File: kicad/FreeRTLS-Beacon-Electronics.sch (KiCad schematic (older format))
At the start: 28 parts, among them J1 USB_B_Micro, J2 TC2030, U1 STM32F072CBTx, U2 AZ1117IH-3.3TRG1, U3 DWM1001

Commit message: Add license info in page settings
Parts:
- D3, D5: Manufacturer Wurth Elektronik -> Würth Elektronik
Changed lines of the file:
@@
 Rev "WIP!"
 Comp "FreeRTLS"
-Comment1 "Revisor: Luciano Vittori"
-Comment2 "Author: David Broin"
-Comment3 ""
-Comment4 ""
+Comment1 ""
+Comment2 "CERN Open Hardware Licence Version 2 - Permissive"
+Comment3 "Revisor: Luciano Vittori"
+Comment4 "Author: David Broin"
 $EndDescr
 $Comp
@@
 F 5 "732-4978-1-ND" H 3900 1600 50  0001 C CNN "Digi-Key_PN"
 F 6 "150060RS75000" H 3900 1600 50  0001 C CNN "MPN"
-F 7 "Wurth Elektronik" H 3900 1600 50  0001 C CNN "Manufacturer"
+F 7 "Würth Elektronik" H 3900 1600 50  0001 C CNN "Manufacturer"
 	1    3900 1600
 	0    -1   -1   0
@@
 F 5 "732-4971-1-ND" H 2150 4850 50  0001 C CNN "Digi-Key_PN"
 F 6 "150060GS75000" H 2150 4850 50  0001 C CNN "MPN"
-F 7 "Wurth Elektronik" H 2150 4850 50  0001 C CNN "Manufacturer"
+F 7 "Würth Elektronik" H 2150 4850 50  0001 C CNN "Manufacturer"
 	1    2150 4850
 	0    -1   -1   0

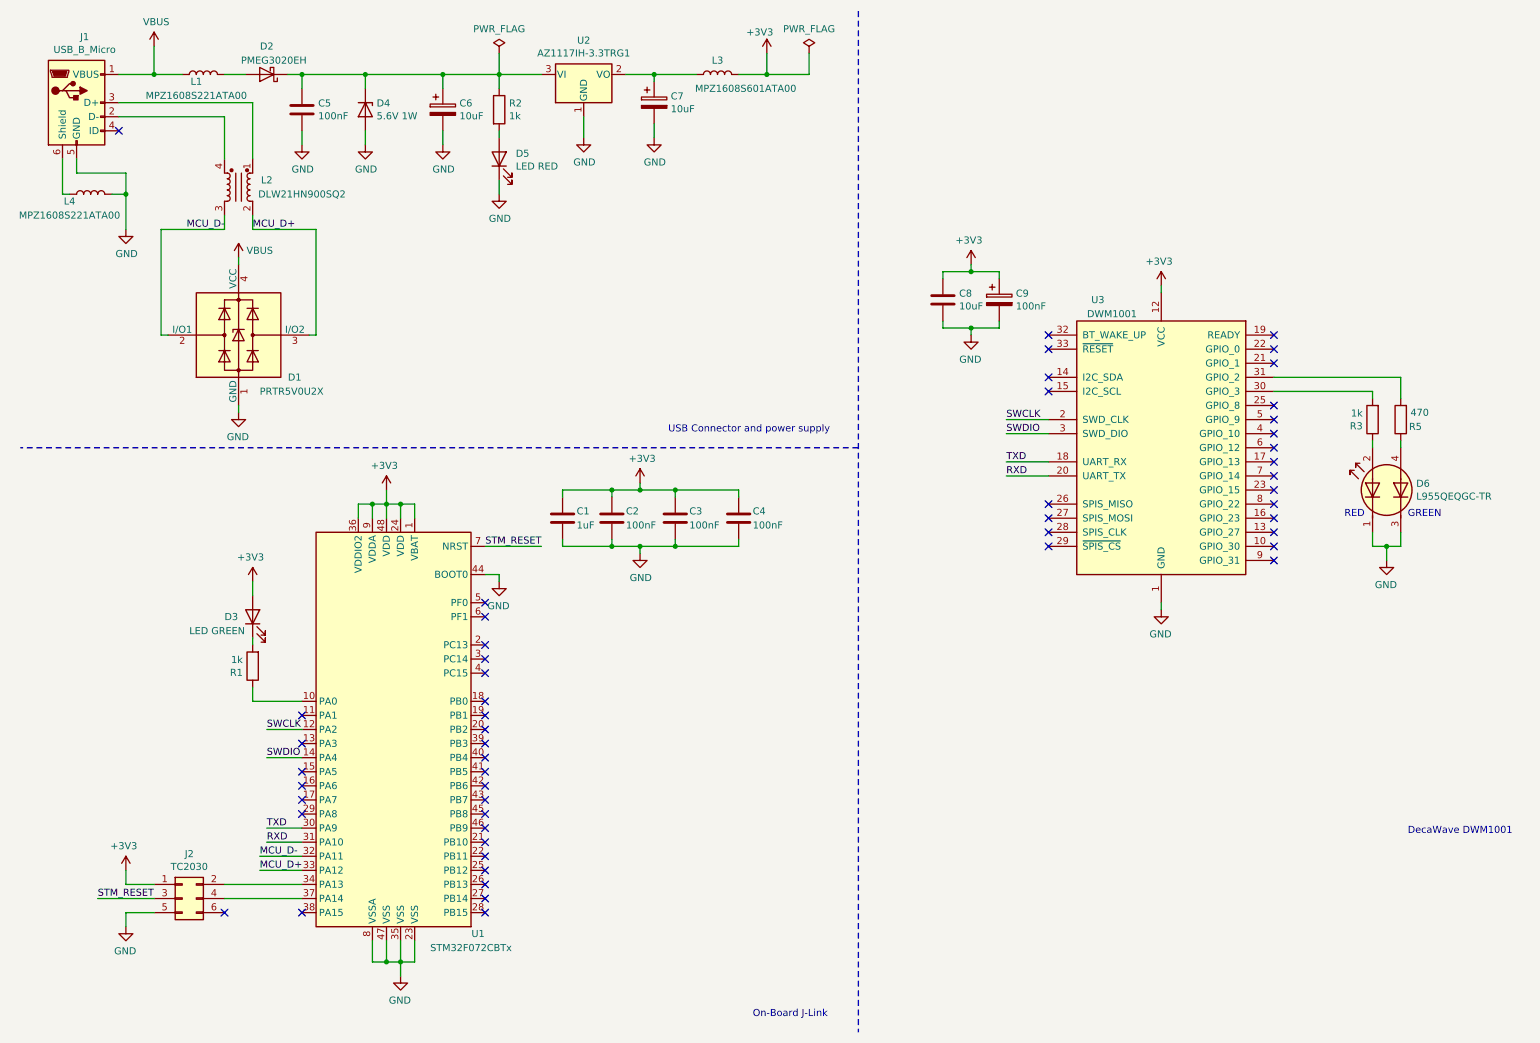
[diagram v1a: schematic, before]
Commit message: Add mounting holes and fiducials
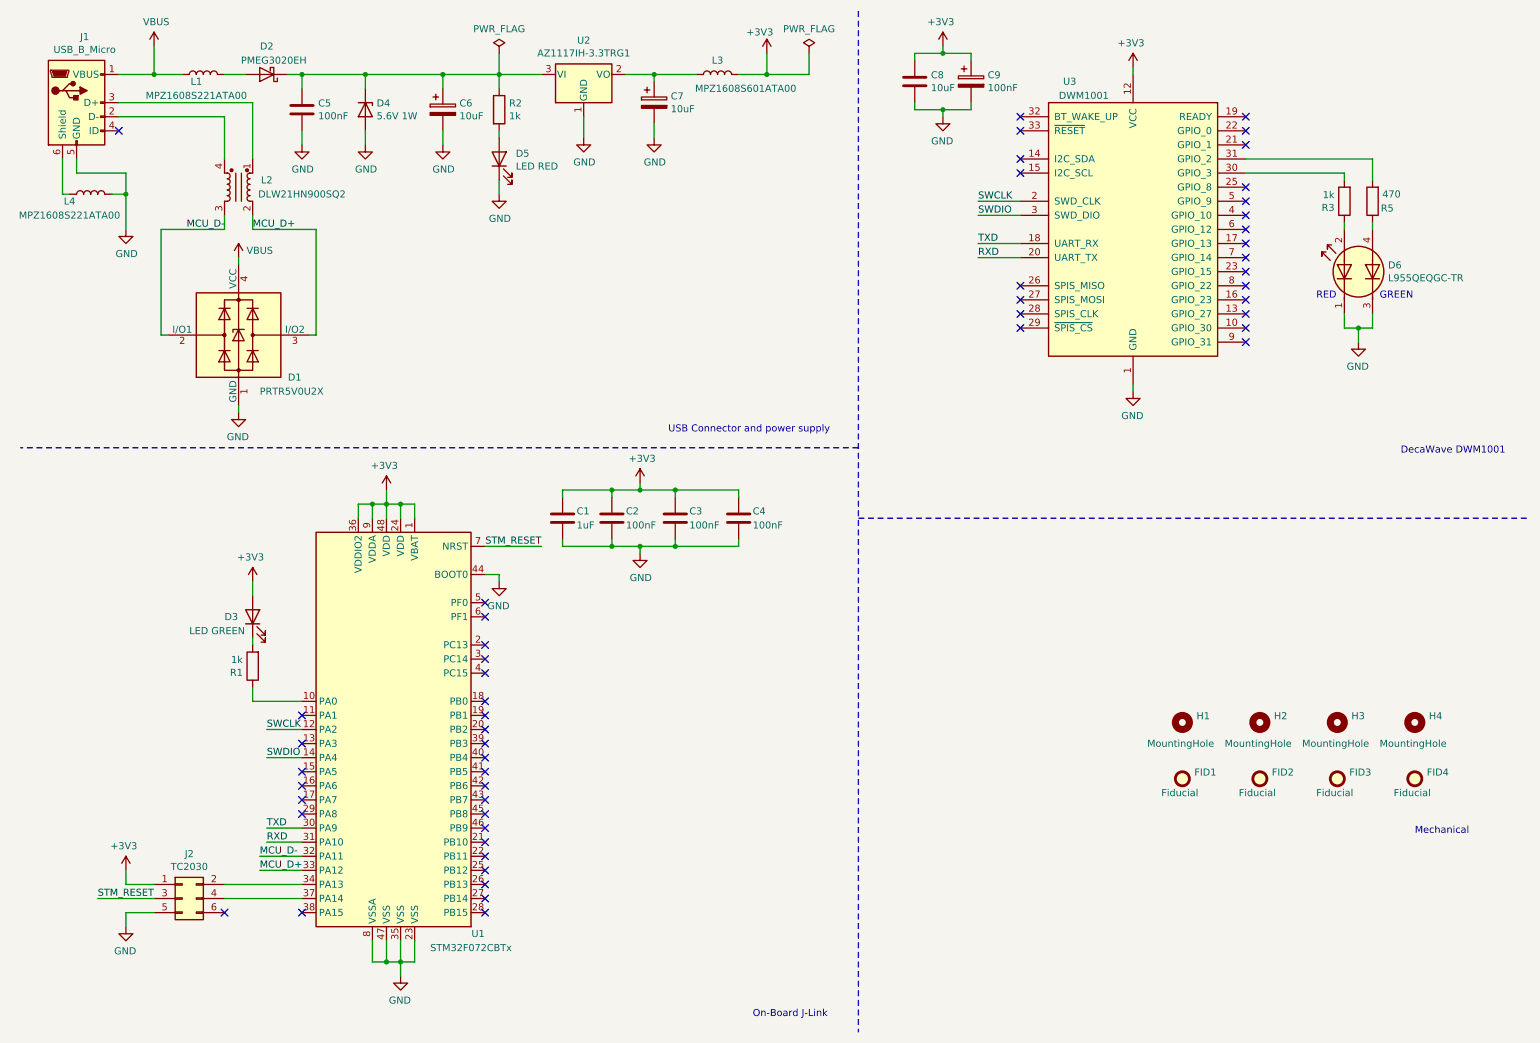
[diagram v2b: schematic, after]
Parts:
- added FID1, FID2, FID3: Fiducial, Fiducial:Fiducial_0.5mm_Mask1.5mm, symbol Mechanical:Fiducial
- added FID4: Fiducial, MountingHole:MountingHole_3.2mm_M3, symbol Mechanical:Fiducial
- added H1, H2, H3, H4: MountingHole, MountingHole:MountingHole_3.2mm_M3, symbol Mechanical:MountingHole
- D3, D5: Manufacturer Würth Elektronik -> Wurth Elektronik
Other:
- note added: "Mechanical"
- moved on the sheet: C8, C9, D6, R3, R5, U3

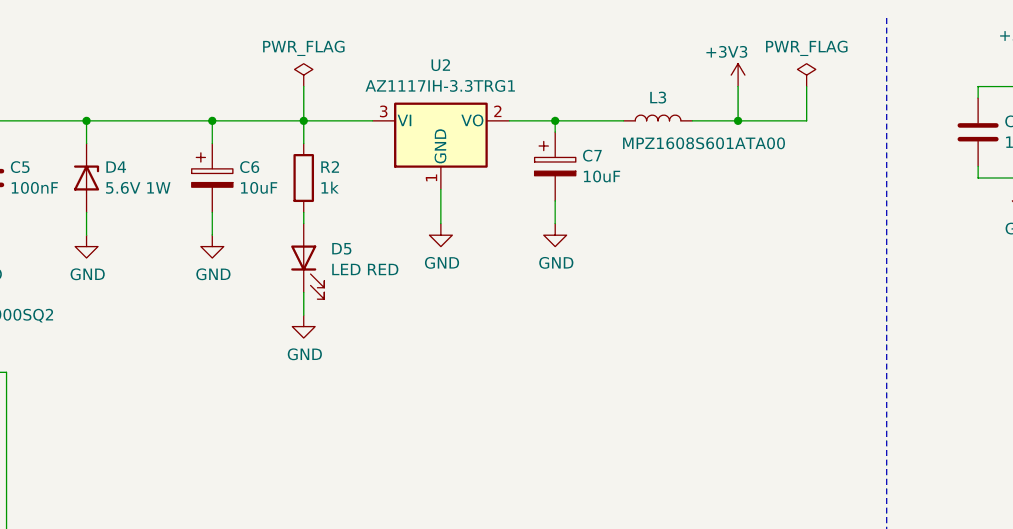
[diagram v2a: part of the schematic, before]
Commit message: Move LED to 3v3 to test whole power
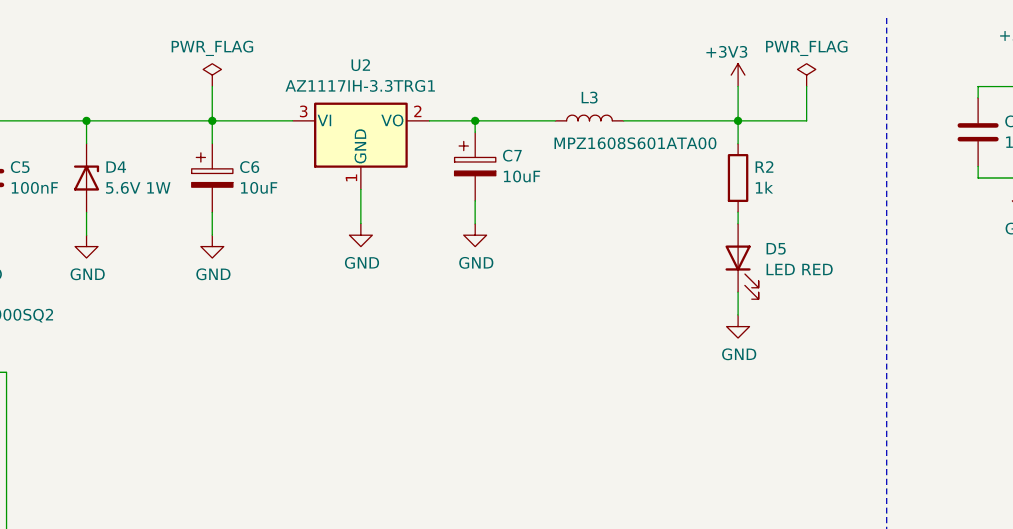
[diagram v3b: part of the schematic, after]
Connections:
- net +3V3: now also R2.1
- net at C5.1, C6.1, D2.1 (K)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: no longer R2.1
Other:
- moved on the sheet: C7, D5, L3, R2, U2
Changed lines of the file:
@@
 L Regulator_Linear:NCP1117-3.3_SOT223 U2
 U 1 1 5F4F1B06
-P 4500 1000
-F 0 "U2" H 4500 1242 50  0000 C CNN
-F 1 "AZ1117IH-3.3TRG1" H 4500 1151 50  0000 C CNN
-F 2 "Package_TO_SOT_SMD:SOT-223-3_TabPin2" H 4500 1200 50  0001 C CNN
-F 3 "https://www.diodes.com/assets/Datasheets/AZ1117I.pdf" H 4600 750 50  0001 C CNN
-F 4 "https://www.digikey.com/en/products/detail/diodes-incorporated/AZ1117IH-3-3TRG1/5699672" H 4500 1000 50  0001 C CNN "DK_Detail_Page"
-F 5 "AZ1117IH-3.3TRG1DICT-ND" H 4500 1000 50  0001 C CNN "Digi-Key_PN"
-F 6 "AZ1117IH-3.3TRG1" H 4500 1000 50  0001 C CNN "MPN"
-F 7 "Diodes Incorporated" H 4500 1000 50  0001 C CNN "Manufacturer"
-	1    4500 1000
+P 4150 1000
+F 0 "U2" H 4150 1242 50  0000 C CNN
+F 1 "AZ1117IH-3.3TRG1" H 4150 1151 50  0000 C CNN
+F 2 "Package_TO_SOT_SMD:SOT-223-3_TabPin2" H 4150 1200 50  0001 C CNN
+F 3 "https://www.diodes.com/assets/Datasheets/AZ1117I.pdf" H 4250 750 50  0001 C CNN
+F 4 "https://www.digikey.com/en/products/detail/diodes-incorporated/AZ1117IH-3-3TRG1/5699672" H 4150 1000 50  0001 C CNN "DK_Detail_Page"
+F 5 "AZ1117IH-3.3TRG1DICT-ND" H 4150 1000 50  0001 C CNN "Digi-Key_PN"
+F 6 "AZ1117IH-3.3TRG1" H 4150 1000 50  0001 C CNN "MPN"
+F 7 "Diodes Incorporated" H 4150 1000 50  0001 C CNN "Manufacturer"
+	1    4150 1000
 	1    0    0    -1
 $EndComp
@@
 	3500 1100 3500 1000
 Connection ~ 3500 1000
-Wire Wire Line
-	3500 1000 3900 1000
 $Comp
 L Device:R R2
 U 1 1 5F4F80D3
-P 3900 1250
-F 0 "R2" H 3970 1296 50  0000 L CNN
-F 1 "1k" H 3970 1205 50  0000 L CNN
-F 2 "Resistor_SMD:R_0603_1608Metric" V 3830 1250 50  0001 C CNN
-F 3 "~" H 3900 1250 50  0001 C CNN
-F 4 "https://www.digikey.com/en/products/detail/yageo/RC0603JR-071KL/726677" H 3900 1250 50  0001 C CNN "DK_Detail_Page"
-F 5 "311-1.0KGRCT-ND" H 3900 1250 50  0001 C CNN "Digi-Key_PN"
-F 6 "RC0603JR-071KL" H 3900 1250 50  0001 C CNN "MPN"
-F 7 "Yageo" H 3900 1250 50  0001 C CNN "Manufacturer"
-	1    3900 1250
+P 5800 1250
+F 0 "R2" H 5870 1296 50  0000 L CNN
+F 1 "1k" H 5870 1205 50  0000 L CNN
+F 2 "Resistor_SMD:R_0603_1608Metric" V 5730 1250 50  0001 C CNN
+F 3 "~" H 5800 1250 50  0001 C CNN
+F 4 "https://www.digikey.com/en/products/detail/yageo/RC0603JR-071KL/726677" H 5800 1250 50  0001 C CNN "DK_Detail_Page"
+F 5 "311-1.0KGRCT-ND" H 5800 1250 50  0001 C CNN "Digi-Key_PN"
+F 6 "RC0603JR-071KL" H 5800 1250 50  0001 C CNN "MPN"
+F 7 "Yageo" H 5800 1250 50  0001 C CNN "Manufacturer"
+	1    5800 1250
 	1    0    0    -1
 $EndComp
@@
 L Device:LED D5
 U 1 1 5F4F882D
-P 3900 1600
-F 0 "D5" V 3939 1482 50  0000 R CNN
-F 1 "LED RED" V 3848 1482 50  0000 R CNN
-F 2 "LED_SMD:LED_0603_1608Metric_Castellated" H 3900 1600 50  0001 C CNN
-F 3 "~" H 3900 1600 50  0001 C CNN
-F 4 "https://www.digikey.com/en/products/detail/w%C3%BCrth-elektronik/150060RS75000/4489901" H 3900 1600 50  0001 C CNN "DK_Detail_Page"
-F 5 "732-4978-1-ND" H 3900 1600 50  0001 C CNN "Digi-Key_PN"
-F 6 "150060RS75000" H 3900 1600 50  0001 C CNN "MPN"
-F 7 "Wurth Elektronik" H 3900 1600 50  0001 C CNN "Manufacturer"
-	1    3900 1600
+P 5800 1600
+F 0 "D5" V 5839 1482 50  0000 R CNN
+F 1 "LED RED" V 5748 1482 50  0000 R CNN
+F 2 "LED_SMD:LED_0603_1608Metric_Castellated" H 5800 1600 50  0001 C CNN
+F 3 "~" H 5800 1600 50  0001 C CNN
+F 4 "https://www.digikey.com/en/products/detail/w%C3%BCrth-elektronik/150060RS75000/4489901" H 5800 1600 50  0001 C CNN "DK_Detail_Page"
+F 5 "732-4978-1-ND" H 5800 1600 50  0001 C CNN "Digi-Key_PN"
+F 6 "150060RS75000" H 5800 1600 50  0001 C CNN "MPN"
+F 7 "Wurth Elektronik" H 5800 1600 50  0001 C CNN "Manufacturer"
+	1    5800 1600
 	0    -1   -1   0
 $EndComp
 Wire Wire Line
-	3900 1100 3900 1000
-Connection ~ 3900 1000
-Wire Wire Line
-	3900 1000 4200 1000
-Wire Wire Line
-	3900 1400 3900 1450
+	5800 1100 5800 1000
+Wire Wire Line
+	3500 1000 3850 1000
+Wire Wire Line
+	5800 1400 5800 1450
 $Comp
 L power:GND #PWR011
@@
 L power:GND #PWR015
 U 1 1 5F4FA5A8
-P 3900 1850
-F 0 "#PWR015" H 3900 1600 50  0001 C CNN
-F 1 "GND" H 3905 1677 50  0000 C CNN
-F 2 "" H 3900 1850 50  0001 C CNN
-F 3 "" H 3900 1850 50  0001 C CNN
-	1    3900 1850
+P 5800 1850
+F 0 "#PWR015" H 5800 1600 50  0001 C CNN
+F 1 "GND" H 5805 1677 50  0000 C CNN
+F 2 "" H 5800 1850 50  0001 C CNN
+F 3 "" H 5800 1850 50  0001 C CNN
+	1    5800 1850
 	1    0    0    -1
 $EndComp
@@
 L power:GND #PWR016
 U 1 1 5F4FAA35
-P 4500 1450
-F 0 "#PWR016" H 4500 1200 50  0001 C CNN
-F 1 "GND" H 4505 1277 50  0000 C CNN
-F 2 "" H 4500 1450 50  0001 C CNN
-F 3 "" H 4500 1450 50  0001 C CNN
-	1    4500 1450
+P 4150 1450
+F 0 "#PWR016" H 4150 1200 50  0001 C CNN
+F 1 "GND" H 4155 1277 50  0000 C CNN
+F 2 "" H 4150 1450 50  0001 C CNN
+F 3 "" H 4150 1450 50  0001 C CNN
+	1    4150 1450
 	1    0    0    -1
 $EndComp
@@
 	3500 1400 3500 1500
 Wire Wire Line
-	3900 1750 3900 1850
-Wire Wire Line
-	4500 1450 4500 1300
+	5800 1750 5800 1850
+Wire Wire Line
+	4150 1450 4150 1300
 $Comp
 L Device:CP C7
 U 1 1 5F4FC537
-P 5000 1200
-F 0 "C7" H 5118 1246 50  0000 L CNN
-F 1 "10uF" H 5118 1155 50  0000 L CNN
-F 2 "Capacitor_SMD:C_0603_1608Metric" H 5038 1050 50  0001 C CNN
-F 3 "~" H 5000 1200 50  0001 C CNN
-F 4 "https://www.digikey.com/en/products/detail/venkel/C0603X6S100-106MNP/12332839" H 5000 1200 50  0001 C CNN "DK_Detail_Page"
-F 5 "2679-C0603X6S100-106MNPTR-ND" H 5000 1200 50  0001 C CNN "Digi-Key_PN"
-F 6 "C0603X6S100-106MNP" H 5000 1200 50  0001 C CNN "MPN"
-F 7 "Venkel" H 5000 1200 50  0001 C CNN "Manufacturer"
-	1    5000 1200
+P 4650 1200
+F 0 "C7" H 4768 1246 50  0000 L CNN
+F 1 "10uF" H 4768 1155 50  0000 L CNN
+F 2 "Capacitor_SMD:C_0603_1608Metric" H 4688 1050 50  0001 C CNN
+F 3 "~" H 4650 1200 50  0001 C CNN
+F 4 "https://www.digikey.com/en/products/detail/venkel/C0603X6S100-106MNP/12332839" H 4650 1200 50  0001 C CNN "DK_Detail_Page"
+F 5 "2679-C0603X6S100-106MNPTR-ND" H 4650 1200 50  0001 C CNN "Digi-Key_PN"
+F 6 "C0603X6S100-106MNP" H 4650 1200 50  0001 C CNN "MPN"
+F 7 "Venkel" H 4650 1200 50  0001 C CNN "Manufacturer"
+	1    4650 1200
 	1    0    0    -1
 $EndComp
@@
 L power:GND #PWR018
 U 1 1 5F4FCE82
-P 5000 1450
-F 0 "#PWR018" H 5000 1200 50  0001 C CNN
-F 1 "GND" H 5005 1277 50  0000 C CNN
-F 2 "" H 5000 1450 50  0001 C CNN
-F 3 "" H 5000 1450 50  0001 C CNN
-	1    5000 1450
+P 4650 1450
+F 0 "#PWR018" H 4650 1200 50  0001 C CNN
+F 1 "GND" H 4655 1277 50  0000 C CNN
+F 2 "" H 4650 1450 50  0001 C CNN
+F 3 "" H 4650 1450 50  0001 C CNN
+	1    4650 1450
 	1    0    0    -1
 $EndComp
@@
 L Device:L L3
 U 1 1 5F4FD73B
-P 5450 1000
-F 0 "L3" V 5550 1000 50  0000 C CNN
-F 1 "MPZ1608S601ATA00" V 5350 800 50  0000 C CNN
-F 2 "Inductor_SMD:L_0603_1608Metric" H 5450 1000 50  0001 C CNN
-F 3 "~" H 5450 1000 50  0001 C CNN
-F 4 "https://www.digikey.com/en/products/detail/tdk-corporation/MPZ1608S601ATA00/765064" H 5450 1000 50  0001 C CNN "DK_Detail_Page"
-F 5 "445-2205-1-ND" H 5450 1000 50  0001 C CNN "Digi-Key_PN"
-F 6 "MPZ1608S601ATA00" H 5450 1000 50  0001 C CNN "MPN"
-F 7 "TDK Corporation" H 5450 1000 50  0001 C CNN "Manufacturer"
-	1    5450 1000
+P 5150 1000
+F 0 "L3" V 5250 1000 50  0000 C CNN
+F 1 "MPZ1608S601ATA00" V 5050 800 50  0000 C CNN
+F 2 "Inductor_SMD:L_0603_1608Metric" H 5150 1000 50  0001 C CNN
+F 3 "~" H 5150 1000 50  0001 C CNN
+F 4 "https://www.digikey.com/en/products/detail/tdk-corporation/MPZ1608S601ATA00/765064" H 5150 1000 50  0001 C CNN "DK_Detail_Page"
+F 5 "445-2205-1-ND" H 5150 1000 50  0001 C CNN "Digi-Key_PN"
+F 6 "MPZ1608S601ATA00" H 5150 1000 50  0001 C CNN "MPN"
+F 7 "TDK Corporation" H 5150 1000 50  0001 C CNN "Manufacturer"
+	1    5150 1000
 	0    -1   -1   0
 $EndComp
 Wire Wire Line
-	4800 1000 5000 1000
-Wire Wire Line
-	5000 1050 5000 1000
-Connection ~ 5000 1000
-Wire Wire Line
-	5000 1000 5300 1000
-Wire Wire Line
-	5000 1350 5000 1450
+	4450 1000 4650 1000
+Wire Wire Line
+	4650 1050 4650 1000
+Connection ~ 4650 1000
+Wire Wire Line
+	4650 1000 5000 1000
+Wire Wire Line
+	4650 1350 4650 1450
 $Comp
 L power:+3V3 #PWR019
@@
 	5800 850  5800 1000
 Wire Wire Line
-	5800 1000 5600 1000
+	5800 1000 5300 1000
 $Comp
 L power:GND #PWR01
@@
 L power:PWR_FLAG #FLG0101
 U 1 1 5F7CC472
-P 3900 850
-F 0 "#FLG0101" H 3900 925 50  0001 C CNN
-F 1 "PWR_FLAG" H 3900 1023 50  0000 C CNN
-F 2 "" H 3900 850 50  0001 C CNN
-F 3 "~" H 3900 850 50  0001 C CNN
-	1    3900 850
-	1    0    0    -1
-$EndComp
-Wire Wire Line
-	3900 850  3900 1000
+P 3500 850
+F 0 "#FLG0101" H 3500 925 50  0001 C CNN
+F 1 "PWR_FLAG" H 3500 1023 50  0000 C CNN
+F 2 "" H 3500 850 50  0001 C CNN
+F 3 "~" H 3500 850 50  0001 C CNN
+	1    3500 850
+	1    0    0    -1
+$EndComp
+Wire Wire Line
+	3500 850  3500 1000
 $Comp
 L power:PWR_FLAG #FLG0102
